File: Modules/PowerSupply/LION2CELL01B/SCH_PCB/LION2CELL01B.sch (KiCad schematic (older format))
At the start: 92 parts

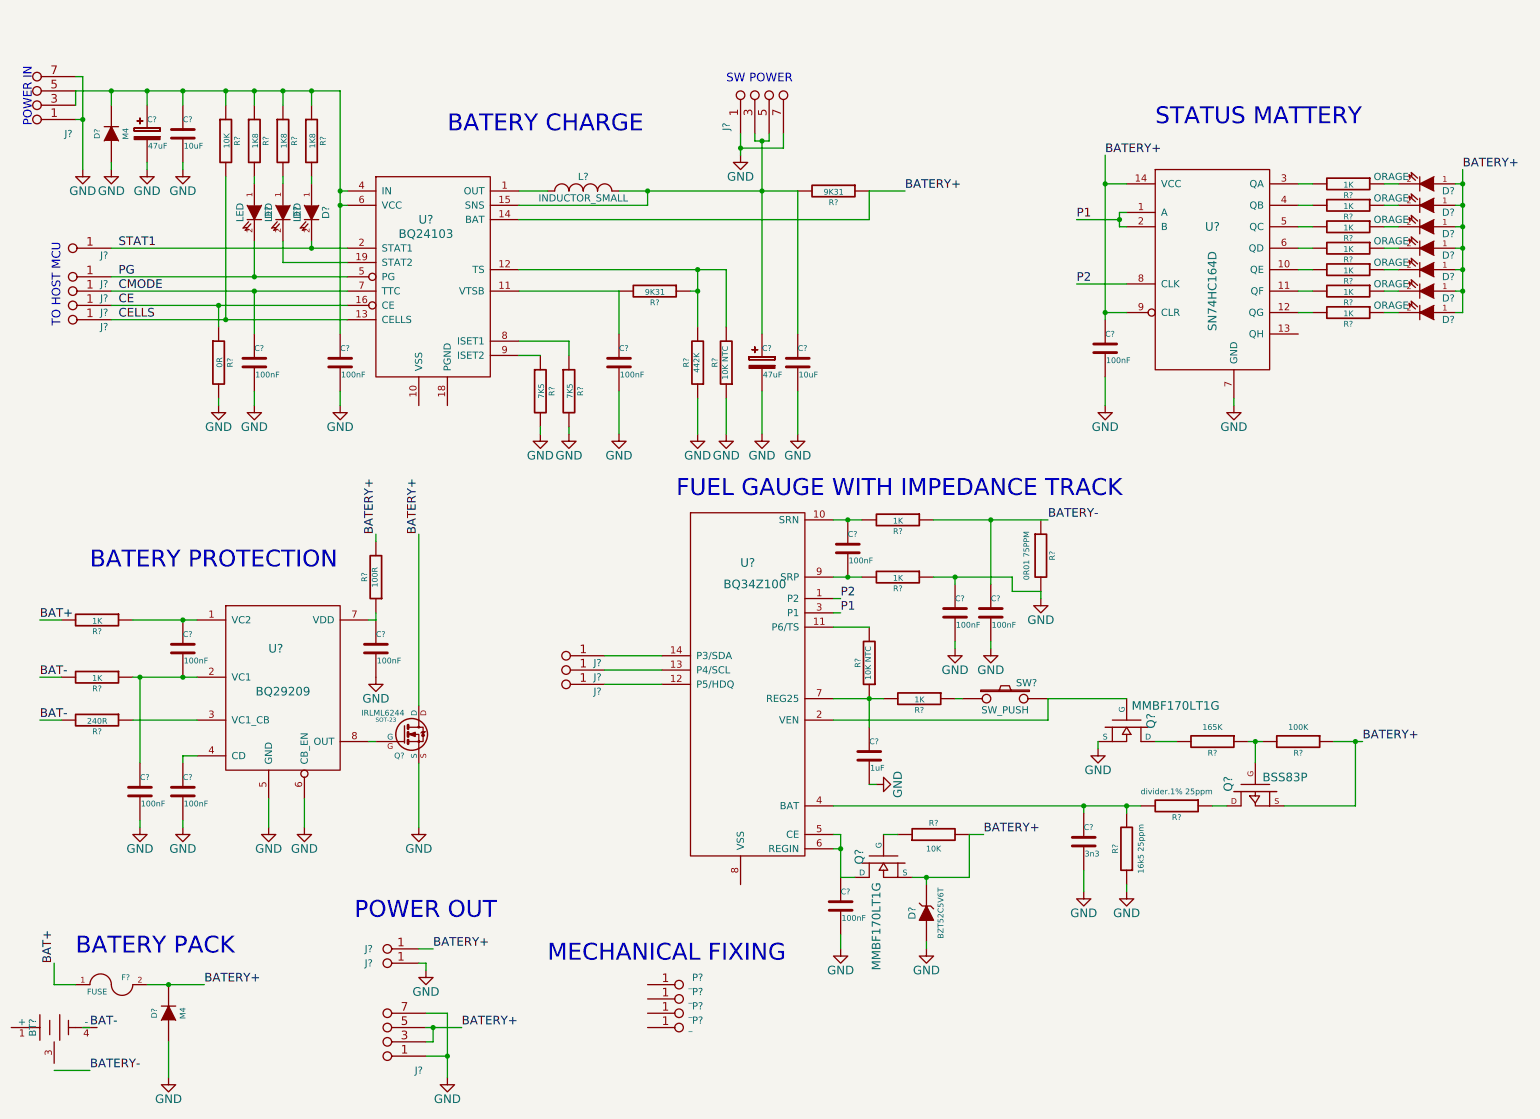
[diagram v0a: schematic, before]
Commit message: 
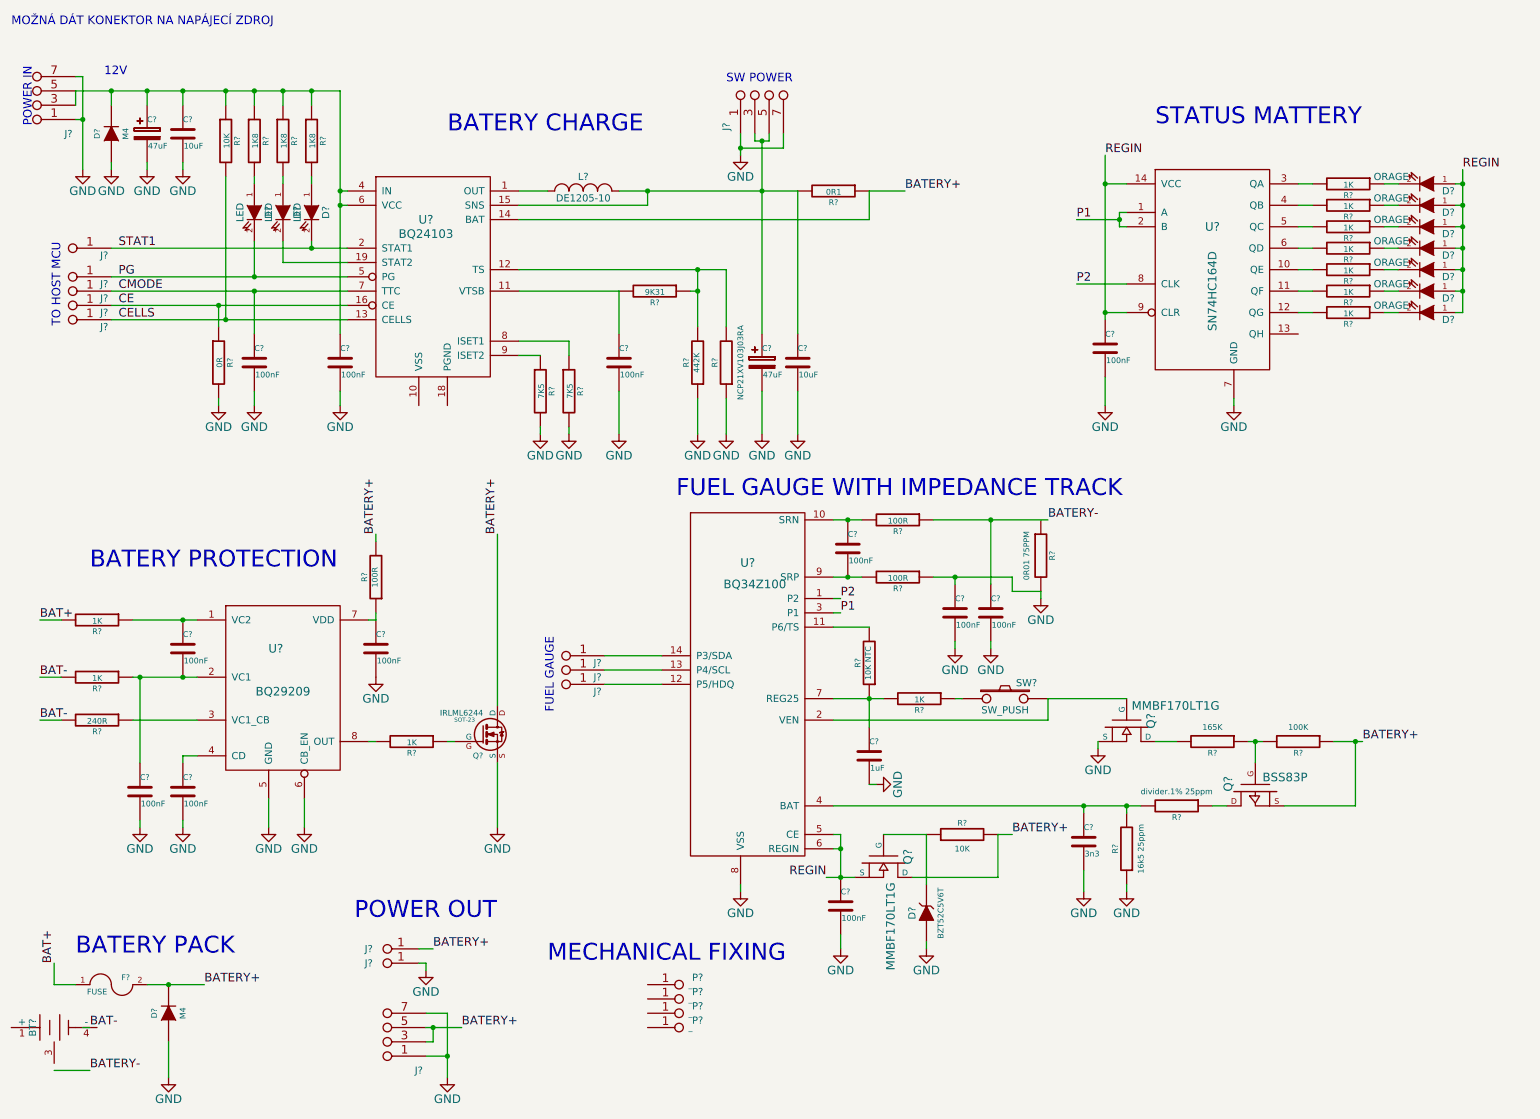
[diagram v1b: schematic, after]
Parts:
- added R?: 1K, symbol R
- L?: value INDUCTOR_SMALL -> DE1205-10
- R?: value 10K NTC -> NCP21XV103J03RA
- R?: value 9K31 -> 0R1
- R? (x2): value 1K -> 100R
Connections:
- net BATERY+: now also Q?.D; no longer C?.1, D?.1 (A), D?.1 (A), D?.1 (A), D?.1 (A), D?.1 (A), D?.1 (A), D?.1 (A), D?.2 (K), Q?.S, U?.14 (VCC), U?.9 (CLR)
- net GND: now also U?.8 (VSS)
- net at U?.8 (OUT): now also R?.2; no longer Q?.G
- net REGIN: now reaches C?.1, U?.5 (CE), U?.6 (REGIN)
- net REGIN: now also C?.1, D?.1 (A), D?.1 (A), D?.1 (A), D?.1 (A), D?.1 (A), D?.1 (A), D?.1 (A), Q?.S, U?.14 (VCC), U?.9 (CLR); no longer Q?.D
- net at Q?.G, R?.1: now also D?.2 (K)
- new net: Q?.G, R?.1
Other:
- note added: "12V"
- note added: "FUEL GAUGE"
- note added: "MOŽNÁ DÁT KONEKTOR NA NAPÁJECÍ ZDROJ"
- moved on the sheet: Q?, R?
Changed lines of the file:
@@
 P 4400 1400
 F 0 "L?" H 4400 1500 50  0000 C CNN
-F 1 "INDUCTOR_SMALL" H 4400 1350 50  0000 C CNN
+F 1 "DE1205-10" H 4400 1350 50  0000 C CNN
 F 2 "" H 4400 1400 60  0000 C CNN
 F 3 "" H 4400 1400 60  0000 C CNN
@@
 P 5400 2600
 F 0 "R?" V 5480 2600 40  0000 C CNN
-F 1 "10K NTC" V 5407 2601 40  0000 C CNN
+F 1 "NCP21XV103J03RA" V 5300 2600 40  0000 C CNN
 F 2 "" V 5330 2600 30  0000 C CNN
 F 3 "" H 5400 2600 30  0000 C CNN
@@
 P 6150 1400
 F 0 "R?" V 6230 1400 40  0000 C CNN
-F 1 "9K31" V 6157 1401 40  0000 C CNN
+F 1 "0R1" V 6157 1401 40  0000 C CNN
 F 2 "" V 6080 1400 30  0000 C CNN
 F 3 "" H 6150 1400 30  0000 C CNN
@@
 L MOSFET-N Q?
 U 1 1 55334750
-P 3150 5200
-F 0 "Q?" H 3150 5051 40  0000 R CNN
-F 1 "IRLML6244" H 3150 5350 40  0000 R CNN
-F 2 "SOT-23" H 3020 5302 29  0000 C CNN
-F 3 "" H 3150 5200 60  0000 C CNN
-	1    3150 5200
+P 3700 5200
+F 0 "Q?" H 3700 5051 40  0000 R CNN
+F 1 "IRLML6244" H 3700 5350 40  0000 R CNN
+F 2 "SOT-23" H 3570 5302 29  0000 C CNN
+F 3 "" H 3700 5200 60  0000 C CNN
+	1    3700 5200
 	1    0    0    -1
 $EndComp
@@
 Text Label 2950 3800 1    60   ~ 0
 BATERY+
-Text Label 3250 3800 1    60   ~ 0
+Text Label 3800 3800 1    60   ~ 0
 BATERY+
 $Comp
 L GND #PWR?
 U 1 1 55337A91
-P 3250 5850
-F 0 "#PWR?" H 3250 5600 60  0001 C CNN
-F 1 "GND" H 3250 5700 60  0000 C CNN
-F 2 "" H 3250 5850 60  0000 C CNN
-F 3 "" H 3250 5850 60  0000 C CNN
-	1    3250 5850
+P 3800 5850
+F 0 "#PWR?" H 3800 5600 60  0001 C CNN
+F 1 "GND" H 3800 5700 60  0000 C CNN
+F 2 "" H 3800 5850 60  0000 C CNN
+F 3 "" H 3800 5850 60  0000 C CNN
+	1    3800 5850
 	1    0    0    -1
 $EndComp
@@
 	-1   0    0    1
 $EndComp
-Text Label 10550 1250 0    60   ~ 0
-BATERY+
 $Comp
 L GND #PWR?
@@
 	1    0    0    -1
 $EndComp
-Text Label 8050 1150 0    60   ~ 0
-BATERY+
 $Comp
 L GND #PWR?
@@
 P 6600 3700
 F 0 "R?" V 6680 3700 40  0000 C CNN
-F 1 "1K" V 6607 3701 40  0000 C CNN
+F 1 "100R" V 6607 3701 40  0000 C CNN
 F 2 "" V 6530 3700 30  0000 C CNN
 F 3 "" H 6600 3700 30  0000 C CNN
@@
 P 6600 4100
 F 0 "R?" V 6680 4100 40  0000 C CNN
-F 1 "1K" V 6607 4101 40  0000 C CNN
+F 1 "100R" V 6607 4101 40  0000 C CNN
 F 2 "" V 6530 4100 30  0000 C CNN
 F 3 "" H 6600 4100 30  0000 C CNN
@@
 F 3 "" H 6500 6100 60  0000 C CNN
 	1    6500 6100
-	0    -1   1    0
+	0    1    1    0
 $EndComp
 $Comp
 L R R?
 U 1 1 553576E2
-P 6850 5900
-F 0 "R?" V 6930 5900 40  0000 C CNN
-F 1 "10K" V 6750 5900 40  0000 C CNN
-F 2 "" V 6780 5900 30  0000 C CNN
-F 3 "" H 6850 5900 30  0000 C CNN
-	1    6850 5900
+P 7050 5900
+F 0 "R?" V 7130 5900 40  0000 C CNN
+F 1 "10K" V 6950 5900 40  0000 C CNN
+F 2 "" V 6980 5900 30  0000 C CNN
+F 3 "" H 7050 5900 30  0000 C CNN
+	1    7050 5900
 	0    -1   -1   0
 $EndComp
-Text Label 7200 5900 0    60   ~ 0
+Text Label 7400 5900 0    60   ~ 0
 BATERY+
 $Comp
@@
 	2950 4400 2950 4350
 Wire Wire Line
-	3250 5000 3250 3800
+	3800 5000 3800 3800
 Wire Wire Line
 	2950 3850 2950 3800
 Wire Wire Line
-	3250 5850 3250 5400
+	3800 5850 3800 5400
 Wire Wire Line
 	7600 4250 7600 4200
@@
 	6400 5550 6450 5550
 Wire Wire Line
-	7100 5900 7100 6200
-Wire Wire Line
-	7100 6200 6700 6200
-Wire Wire Line
-	7100 5900 7200 5900
-Wire Wire Line
-	6800 6250 6800 6200
-Connection ~ 6800 6200
-Wire Wire Line
-	6600 5900 6500 5900
+	7300 6200 7300 5900
+Wire Wire Line
+	6700 6200 7300 6200
+Wire Wire Line
+	7300 5900 7400 5900
+Wire Wire Line
+	6500 5900 6800 5900
 Wire Wire Line
 	6150 5900 6200 5900
@@
 Connection ~ 6200 6000
 Wire Wire Line
-	6200 6200 6300 6200
+	6100 6200 6300 6200
 Wire Wire Line
 	6800 6700 6800 6650
@@
 Text Notes 8400 950  0    118  ~ 0
 STATUS MATTERY
+Connection ~ 6200 6200
+Text Label 6100 6200 2    60   ~ 0
+REGIN
+Text Label 8050 1150 0    60   ~ 0
+REGIN
+Text Label 10550 1250 0    60   ~ 0
+REGIN
+Wire Wire Line
+	6800 5900 6800 6250
+Text Notes 1050 600  0    60   ~ 0
+12V
+Text Notes 400  250  0    60   ~ 0
+MOŽNÁ DÁT KONEKTOR NA NAPÁJECÍ ZDROJ
+$Comp
+L R R?
+U 1 1 5533B935
+P 3200 5250
+F 0 "R?" V 3280 5250 40  0000 C CNN
+F 1 "1K" V 3207 5251 40  0000 C CNN
+F 2 "" V 3130 5250 30  0000 C CNN
+F 3 "" H 3200 5250 30  0000 C CNN
+	1    3200 5250
+	0    1    1    0
+$EndComp
+Wire Wire Line
+	3450 5250 3500 5250
+$Comp
+L GND #PWR?
+U 1 1 553511CC
+P 5500 6300
+F 0 "#PWR?" H 5500 6050 60  0001 C CNN
+F 1 "GND" H 5500 6150 60  0000 C CNN
+F 2 "" H 5500 6300 60  0000 C CNN
+F 3 "" H 5500 6300 60  0000 C CNN
+	1    5500 6300
+	1    0    0    -1
+$EndComp
+Wire Wire Line
+	5500 6300 5500 6250
+Text Notes 4200 5050 1    60   ~ 0
+FUEL GAUGE
 $EndSCHEMATC

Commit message: 
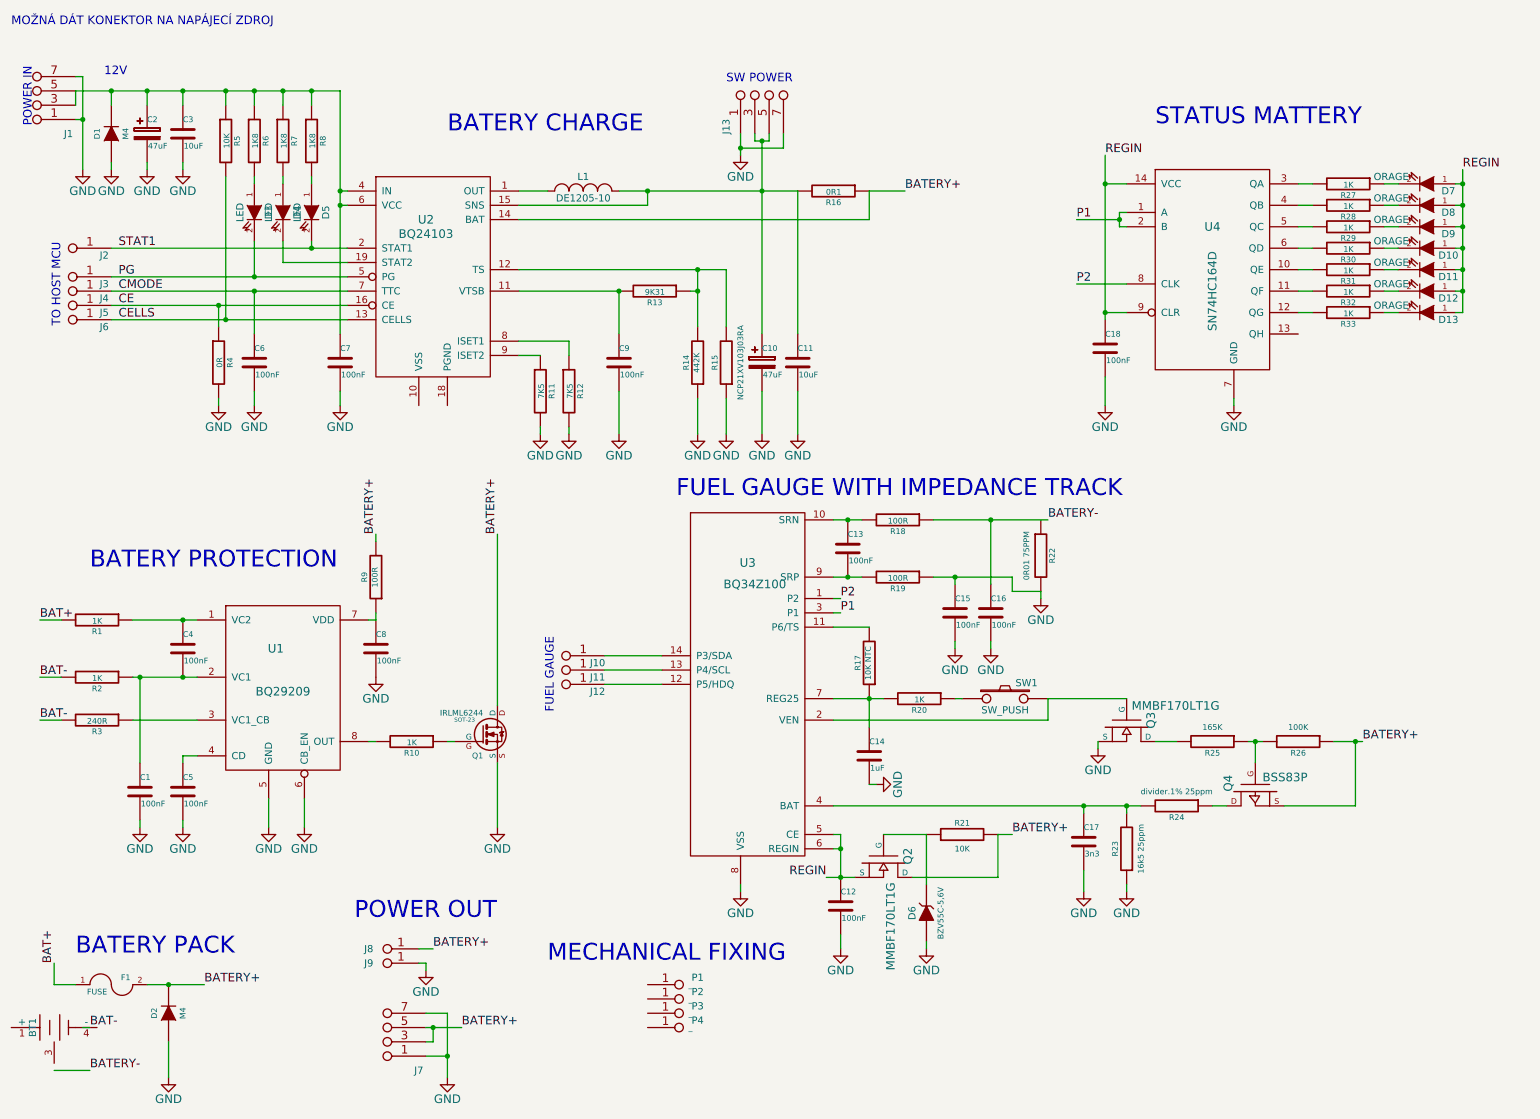
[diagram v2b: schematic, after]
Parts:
- D6: renamed from D?; value BZT52C5V6T -> BZV55C-5,6V; footprint (none) -> Mlab_D:MiniMELF_Standard
- L1: renamed from L?; footprint (none) -> Mlab_L:DE1205-10
- gave numbers to parts that had none: 91

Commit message: 
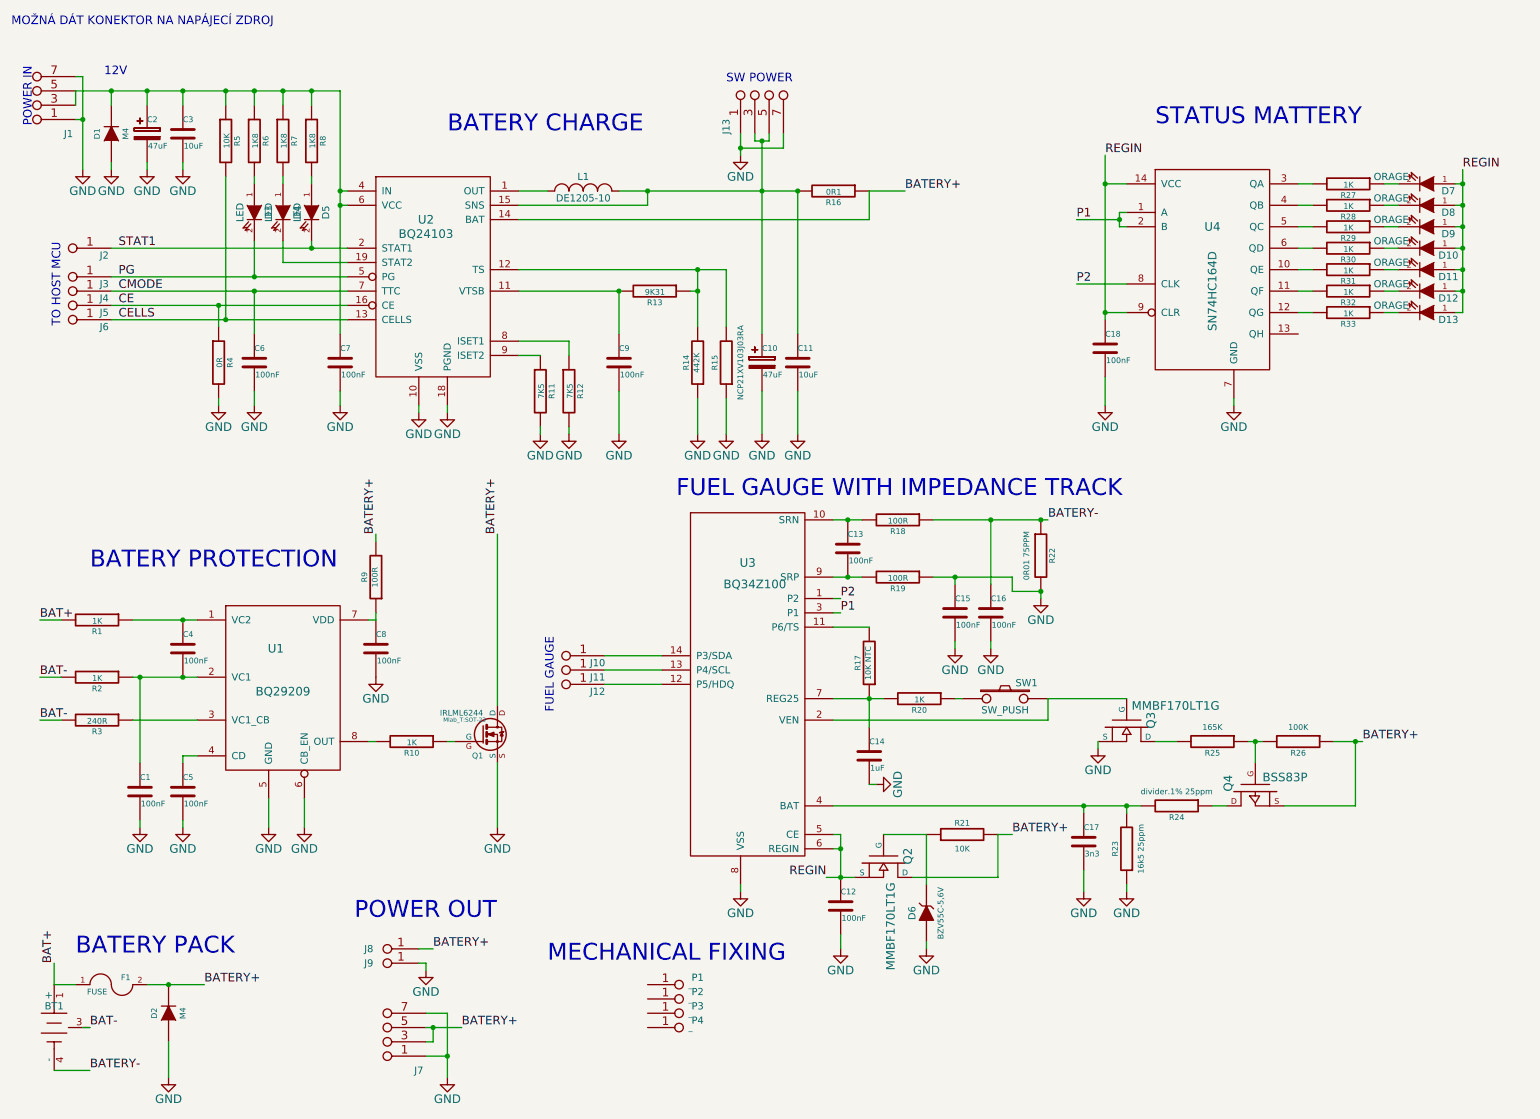
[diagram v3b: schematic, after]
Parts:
- BT1: footprint (none) -> Mlab_Batery:2LION
- C1, C11, C12, C13, C14, C15, C16, C17, C18, C3, C4, C5, C6, C7, C8, C9, R1, R10, R11, R12, R13, R14, R15, R17, R18, R19, R2, R20, R21, R23, R24, R25, R26, R27, R28, R29, R3, R30, R31, R32, R33, R4, R5, R6, R7, R8, R9: footprint (none) -> Mlab_R:SMD-0805
- C10, C2: footprint (none) -> Mlab_C:TantalC_SizeC_Reflow
- D1, D2: footprint (none) -> Mlab_D:SMA_Standard
- D10, D11, D12, D13, D3, D4, D5, D7, D8, D9: footprint (none) -> Mlab_D:LED_1206
- F1: footprint (none) -> Mlab_F:2410
- J1, J13, J7: footprint (none) -> Mlab_Pin_Headers:Straight_2x04
- J10, J11, J12, J2, J3, J4, J5, J6: footprint (none) -> Mlab_Pin_Headers:Straight_1x02
- J8, J9: footprint (none) -> Mlab_Con:WAGO256
- P1, P2, P3, P4: footprint (none) -> Mlab_Mechanical:MountingHole_3mm
- Q1: footprint SOT-23 -> Mlab_T:SOT-23
- Q2, Q3, Q4: footprint (none) -> Mlab_T:SOT-23
- R16: footprint (none) -> Resistors_SMD:R_2512
- R22: footprint (none) -> Mlab_R:SMD-1206
- SW1: footprint (none) -> Mlab_SW:SW_PUSH_SMALL
- U1: footprint (none) -> Mlab_IO:VSON-8
- U2: footprint (none) -> Mlab_IO:VQFN-20
- U3: footprint (none) -> Mlab_IO:TSSOP-14_4.4x5mm_Pitch0.65mm
- U4: footprint (none) -> Mlab_IO:SO-14
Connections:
- net BAT+: now also BT1.1 (+)
- net BAT-: now also BT1.2, BT1.3
- net BATERY-: now also BT1.4 (-), R22.1
- net GND: now also U2.10 (VSS), U2.17 (PGND), U2.18 (PGND), U2.21 (pgnd)
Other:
- moved on the sheet: BT1
